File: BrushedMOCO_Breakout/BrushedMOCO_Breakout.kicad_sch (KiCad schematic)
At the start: 24 parts, among them Q1 Si4156DY, Q2 Si4156DY, Q3 Si4156DY, Q4 Si4156DY, U1 74LVC2G04, U2 IRS2308, U5 IRS2308

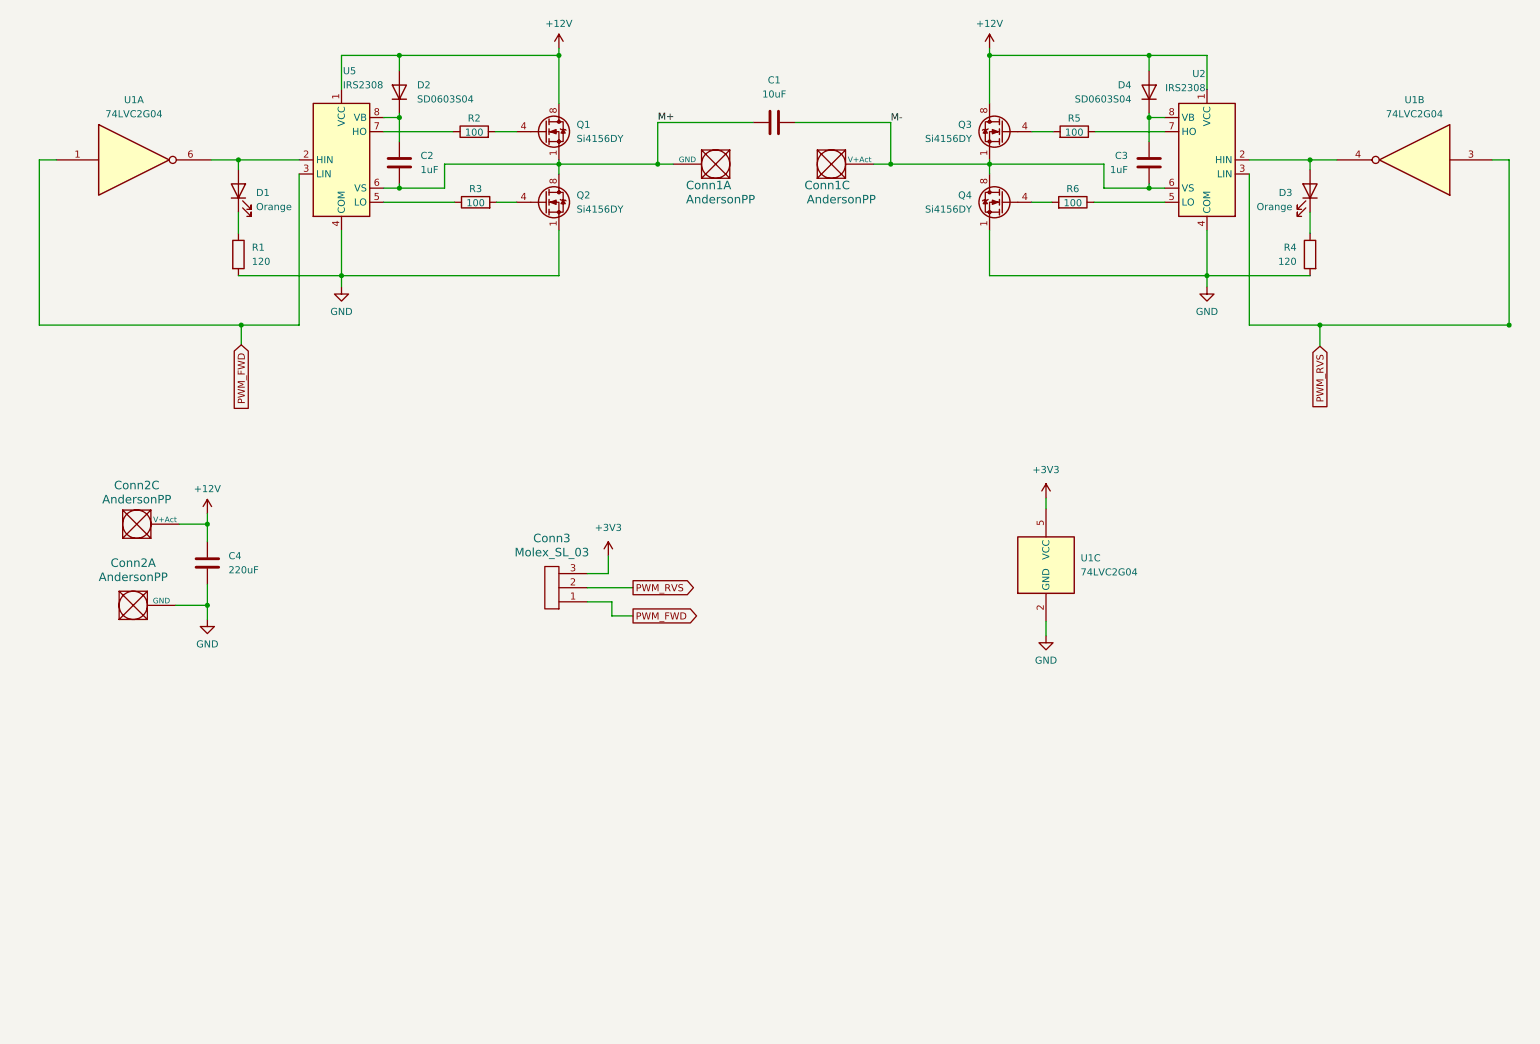
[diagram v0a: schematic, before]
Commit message: Most of Schematic Review Adjustments
This should be all of the schematic review adjustments except for the footprints for the IRS2308. I wasn't sure whether to use
Package_DFN_QFN:Infineon_MLPQ-48-1EP_7x7mm_P0.5mm_EP5.55x5.55mm
or
Package_DFN_QFN:Infineon_MLPQ-48-1EP_7x7mm_P0.5mm_EP5.15x5.15mm
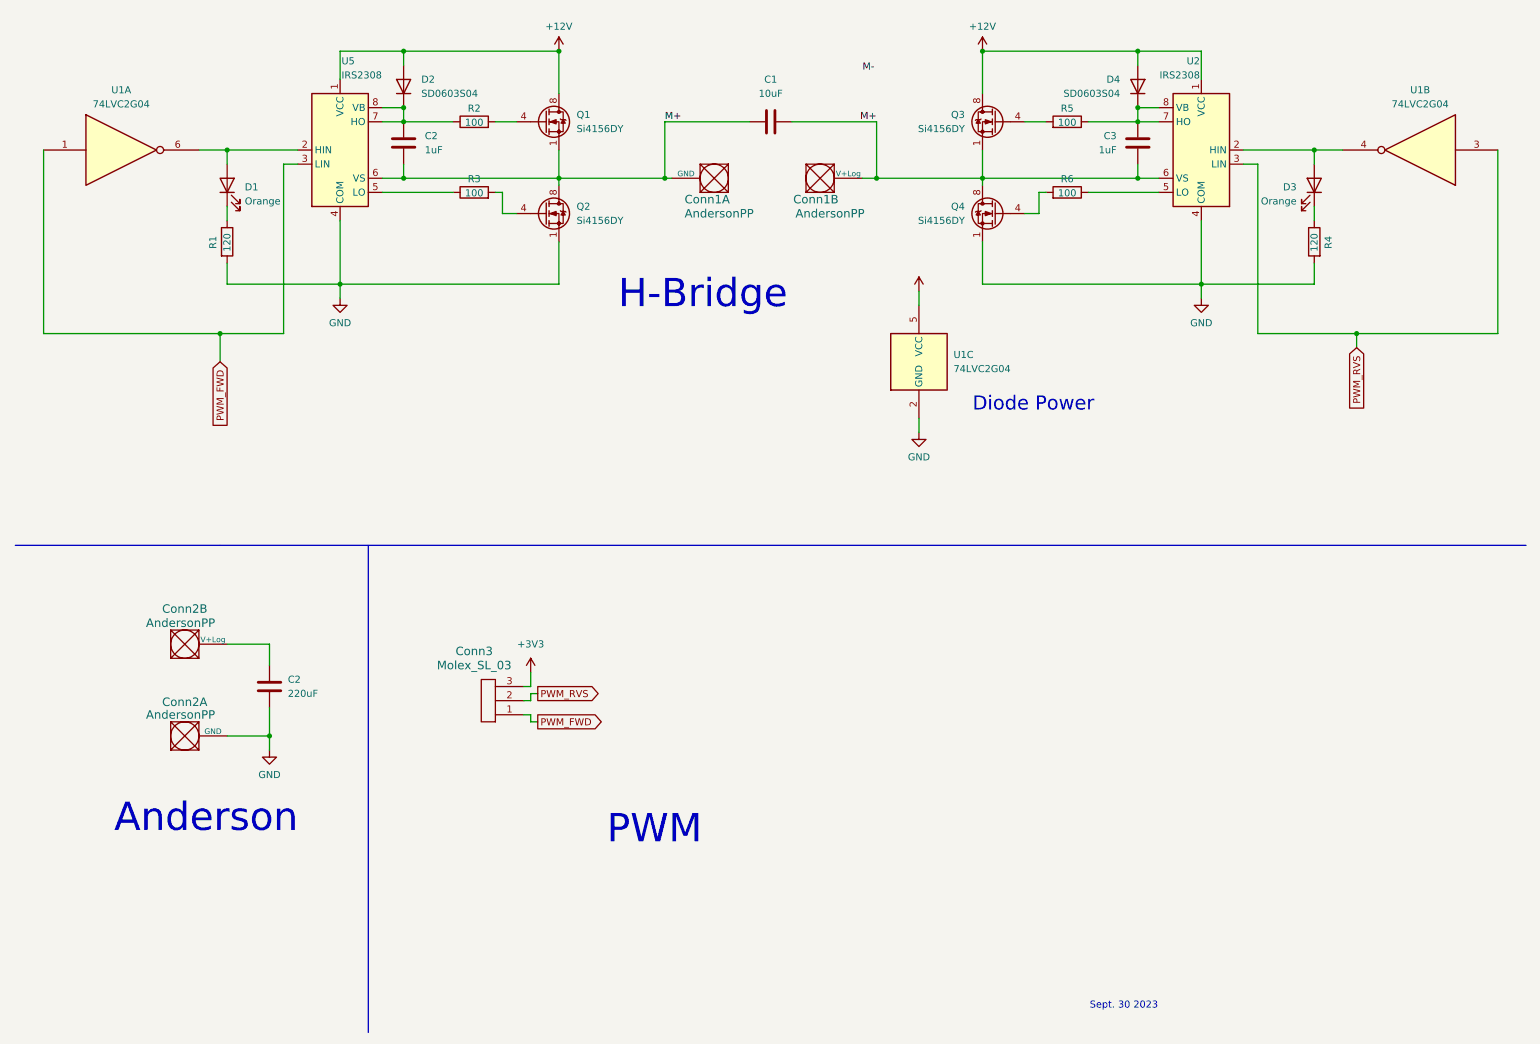
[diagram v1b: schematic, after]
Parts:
- removed unit 3 of Conn2
- added unit 2 of Conn2
- Conn1, Conn2: footprint (none) -> MRDT_Connectors:Square_Anderson_2_H_Side_By_Side_PV
- renumbered C4 to C2
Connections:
- net +12V: no longer C2.2
- net M+: now also C1.2, C3.2, Conn1.2 (V+Log), Q3.1 (S), Q3.2 (S), Q3.3 (S), Q4.5 (D), Q4.6 (D), Q4.7 (D), Q4.8 (D), U2.6 (VS)
- net M-: no longer C1.2, C3.2, Conn1.3 (V+Act), Q3.1 (S), Q3.2 (S), Q3.3 (S), Q4.5 (D), Q4.6 (D), Q4.7 (D), Q4.8 (D), U2.6 (VS)
- net at C2.1, D2.1 (K), U5.8 (VB): now also R2.1, U5.7 (HO)
- net at C3.1, D4.1 (K), U2.8 (VB): now also R5.1, U2.7 (HO)
- new net: C2.2, Conn2.2 (V+Log)
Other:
- note added: "Anderson"
- note added: "Diode Power"
- note added: "H-Bridge"
- note added: "PWM"
- note added: "Sept. 30 2023"
- moved on the sheet: C1, C2, Conn1A, Conn1B, Conn2A, Conn3, D1, D2, Q1, Q2, R1, R2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

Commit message: Finished Footprints
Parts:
- U2: renamed from U5; footprint (none) -> Package_SO:SOIC-8-1EP_3.9x4.9mm_P1.27mm_EP2.29x3mm
- U3: renamed from U2; footprint (none) -> Package_SO:SOIC-8-1EP_3.9x4.9mm_P1.27mm_EP2.29x3mm
- renumbered C2 to C1, C1 to C3, C3 to C4, Conn2 to Conn1, Conn3 to Conn2, Conn1 to Conn3, D4 to D3, D3 to D4, R5 to R4, R6 to R5, R4 to R6
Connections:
- net M+: no longer C3.2, C4.2, Conn3.2 (V+Log), Q3.1 (S), Q3.2 (S), Q3.3 (S), Q4.5 (D), Q4.6 (D), Q4.7 (D), Q4.8 (D), U3.6 (VS)
- net M-: now also C3.2, C4.2, Conn3.2 (V+Log), Q3.1 (S), Q3.2 (S), Q3.3 (S), Q4.5 (D), Q4.6 (D), Q4.7 (D), Q4.8 (D), U3.6 (VS)

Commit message: cleaned up lines
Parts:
- renumbered Conn3 to Conn2
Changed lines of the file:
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@@
     (stroke (width 0) (type default))
   )
-  (polyline (pts (xy 49.53 110.49) (xy 284.48 110.49))
+  (polyline (pts (xy 11.938 109.982) (xy 284.988 109.982))
     (stroke (width 0) (type default))
   )
@@
     (stroke (width 0) (type default))
   )
-  (polyline (pts (xy 12.7 110.49) (xy 49.53 110.49))
-    (stroke (width 0) (type default))
-  )
   (wire (pts (xy 58.42 144.78) (xy 58.42 139.7))
     (stroke (width 0) (type default))
@@
     (stroke (width 0) (type default))
   )
+  (polyline (pts (xy 76.2 197.612) (xy 76.2 197.866))
+    (stroke (width 0) (type default))
+  )
   (wire (pts (xy 218.44 34.29) (xy 214.63 34.29))
     (stroke (width 0) (type default))
@@
     (stroke (width 0) (type default))
   )
-  (polyline (pts (xy 76.2 110.49) (xy 76.2 198.12))
+  (polyline (pts (xy 76.2 109.982) (xy 76.2 197.866))
     (stroke (width 0) (type default))
   )
@@
   )
   (wire (pts (xy 233.68 41.91) (xy 236.22 41.91))
+    (stroke (width 0) (type default))
+  )
+  (polyline (pts (xy 283.972 109.982) (xy 284.988 109.982))
     (stroke (width 0) (type default))
   )
@@
   (symbol (lib_id "MRDT_Connectors:AndersonPP") (at 140.97 41.91 180) (unit 1)
     (in_bom yes) (on_board yes) (dnp no)
-    (property "Reference" "Conn3" (at 133.096 48.26 0)
+    (property "Reference" "Conn2" (at 133.096 48.26 0)
       (effects (font (size 1.524 1.524)) (justify right))
     )
@@
       (project "BrushedMOCO_Breakout"
         (path "/09f10023-b6cf-44c5-8847-9c4a76610e70"
-          (reference "Conn3") (unit 1)
+          (reference "Conn2") (unit 1)
         )
       )
@@
   (symbol (lib_id "MRDT_Connectors:AndersonPP") (at 154.94 46.99 0) (unit 2)
     (in_bom yes) (on_board yes) (dnp no)
-    (property "Reference" "Conn3" (at 156.718 48.26 0)
+    (property "Reference" "Conn2" (at 156.718 48.26 0)
       (effects (font (size 1.524 1.524)))
     )
@@
       (project "BrushedMOCO_Breakout"
         (path "/09f10023-b6cf-44c5-8847-9c4a76610e70"
-          (reference "Conn3") (unit 2)
-        )
-      )
+          (reference "Conn2") (unit 2)
+        )
+      )

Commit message: Saving PCB Progress
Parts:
- renumbered Conn2 to Conn3
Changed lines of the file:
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@@
-    )
-  )
-  (symbol (lib_id "MRDT_Connectors:AndersonPP") (at 140.97 41.91 180) (unit 1)
-    (in_bom yes) (on_board yes) (dnp no)
-    (property "Reference" "Conn2" (at 133.096 48.26 0)
-      (effects (font (size 1.524 1.524)) (justify right))
-    )
-    (property "Value" "AndersonPP" (at 133.096 50.8 0)
-      (effects (font (size 1.524 1.524)) (justify right))
-    )
-    (property "Footprint" "MRDT_Connectors:Square_Anderson_2_H_Side_By_Side_PV" (at 144.78 27.94 0)
-      (effects (font (size 1.524 1.524)) hide)
-    )
-    (property "Datasheet" "" (at 144.78 27.94 0)
-      (effects (font (size 1.524 1.524)) hide)
-    )
-    (pin "1")
-    (pin "2")
-    (pin "3")
-    (pin "4")
-    (pin "1")
-    (instances
-      (project "BrushedMOCO_Breakout"
-        (path "/09f10023-b6cf-44c5-8847-9c4a76610e70"
-          (reference "Conn2") (unit 1)
-        )
-      )
     )
   )
@@
     )
   )
-  (symbol (lib_id "power:+3V3") (at 175.26 64.77 0) (mirror y) (unit 1)
-    (in_bom yes) (on_board yes) (dnp no) (fields_autoplaced)
-    (property "Reference" "#PWR05" (at 175.26 68.58 0)
+  (symbol (lib_id "Device:R") (at 95.25 34.29 90) (unit 1)
+    (in_bom yes) (on_board yes) (dnp no)
+    (property "Reference" "R2" (at 95.25 31.877 90)
+      (effects (font (size 1.27 1.27)))
+    )
+    (property "Value" "100" (at 95.25 34.417 90)
+      (effects (font (size 1.27 1.27)))
+    )
+    (property "Footprint" "Resistor_SMD:R_0603_1608Metric_Pad0.98x0.95mm_HandSolder" (at 95.25 36.068 90)
+      (effects (font (size 1.27 1.27)) hide)
+    )
+    (property "Datasheet" "~" (at 95.25 34.29 0)
+      (effects (font (size 1.27 1.27)) hide)
+    )
+    (pin "1")
+    (pin "2")
+    (instances
+      (project "BrushedMOCO_Breakout"
+        (path "/09f10023-b6cf-44c5-8847-9c4a76610e70"
+          (reference "R2") (unit 1)
+        )
+      )
+    )
+  )
+  (symbol (lib_id "power:GND") (at 175.26 90.17 0) (unit 1)
+    (in_bom yes) (on_board yes) (dnp no) (fields_autoplaced)
+    (property "Reference" "#PWR06" (at 175.26 96.52 0)
+      (effects (font (size 1.27 1.27)) hide)
+    )
+    (property "Value" "GND" (at 175.26 94.615 0)
+      (effects (font (size 1.27 1.27)))
+    )
+    (property "Footprint" "" (at 175.26 90.17 0)
+      (effects (font (size 1.27 1.27)) hide)
+    )
+    (property "Datasheet" "" (at 175.26 90.17 0)
+      (effects (font (size 1.27 1.27)) hide)
+    )
+    (pin "1")
+    (instances
+      (project "BrushedMOCO_Breakout"
+        (path "/09f10023-b6cf-44c5-8847-9c4a76610e70"
+          (reference "#PWR06") (unit 1)
+        )
+      )
+    )
+  )
+  (symbol (lib_id "74xGxx:74LVC2G04") (at 175.26 77.47 0) (unit 3)
+    (in_bom yes) (on_board yes) (dnp no) (fields_autoplaced)
+    (property "Reference" "U1" (at 181.483 76.2 0)
+      (effects (font (size 1.27 1.27)) (justify left))
+    )
+    (property "Value" "74LVC2G04" (at 181.483 78.74 0)
+      (effects (font (size 1.27 1.27)) (justify left))
+    )
+    (property "Footprint" "Package_TO_SOT_SMD:SOT-23-6_Handsoldering" (at 175.26 77.47 0)
+      (effects (font (size 1.27 1.27)) hide)
+    )
+    (property "Datasheet" "http://www.ti.com/lit/sg/scyt129e/scyt129e.pdf" (at 175.26 77.47 0)
+      (effects (font (size 1.27 1.27)) hide)
+    )
+    (pin "1")
+    (pin "6")
+    (pin "3")
+    (pin "4")
+    (pin "2")
+    (pin "5")
+    (instances
+      (project "BrushedMOCO_Breakout"
+        (path "/09f10023-b6cf-44c5-8847-9c4a76610e70"
+          (reference "U1") (unit 3)
+        )
+      )
+    )
+  )
+  (symbol (lib_id "power:+3V3") (at 175.26 64.77 0) (unit 1)
+    (in_bom yes) (on_board yes) (dnp no) (fields_autoplaced)
+    (property "Reference" "#PWR09" (at 175.26 68.58 0)
       (effects (font (size 1.27 1.27)) hide)
     )
     (property "Value" "+3V3" (at 175.26 59.69 0)
-      (effects (font (size 1.27 1.27)) hide)
+      (effects (font (size 1.27 1.27)))
     )
     (property "Footprint" "" (at 175.26 64.77 0)
@@
       (project "BrushedMOCO_Breakout"
         (path "/09f10023-b6cf-44c5-8847-9c4a76610e70"
-          (reference "#PWR05") (unit 1)
-        )
-      )
-    )
-  )
-  (symbol (lib_id "Device:R") (at 95.25 34.29 90) (unit 1)
-    (in_bom yes) (on_board yes) (dnp no)
-    (property "Reference" "R2" (at 95.25 31.877 90)
-      (effects (font (size 1.27 1.27)))
-    )
-    (property "Value" "100" (at 95.25 34.417 90)
-      (effects (font (size 1.27 1.27)))
-    )
-    (property "Footprint" "Resistor_SMD:R_0603_1608Metric_Pad0.98x0.95mm_HandSolder" (at 95.25 36.068 90)
-      (effects (font (size 1.27 1.27)) hide)
-    )
-    (property "Datasheet" "~" (at 95.25 34.29 0)
-      (effects (font (size 1.27 1.27)) hide)
-    )
-    (pin "1")
-    (pin "2")
-    (instances
-      (project "BrushedMOCO_Breakout"
-        (path "/09f10023-b6cf-44c5-8847-9c4a76610e70"
-          (reference "R2") (unit 1)
-        )
-      )
-    )
-  )
-  (symbol (lib_id "power:GND") (at 175.26 90.17 0) (unit 1)
-    (in_bom yes) (on_board yes) (dnp no) (fields_autoplaced)
-    (property "Reference" "#PWR06" (at 175.26 96.52 0)
-      (effects (font (size 1.27 1.27)) hide)
-    )
-    (property "Value" "GND" (at 175.26 94.615 0)
-      (effects (font (size 1.27 1.27)))
-    )
-    (property "Footprint" "" (at 175.26 90.17 0)
-      (effects (font (size 1.27 1.27)) hide)
-    )
-    (property "Datasheet" "" (at 175.26 90.17 0)
-      (effects (font (size 1.27 1.27)) hide)
-    )
-    (pin "1")
-    (instances
-      (project "BrushedMOCO_Breakout"
-        (path "/09f10023-b6cf-44c5-8847-9c4a76610e70"
-          (reference "#PWR06") (unit 1)
-        )
-      )
-    )
-  )
-  (symbol (lib_id "74xGxx:74LVC2G04") (at 175.26 77.47 0) (unit 3)
-    (in_bom yes) (on_board yes) (dnp no) (fields_autoplaced)
-    (property "Reference" "U1" (at 181.483 76.2 0)
-      (effects (font (size 1.27 1.27)) (justify left))
-    )
-    (property "Value" "74LVC2G04" (at 181.483 78.74 0)
-      (effects (font (size 1.27 1.27)) (justify left))
-    )
-    (property "Footprint" "Package_TO_SOT_SMD:SOT-23-6_Handsoldering" (at 175.26 77.47 0)
-      (effects (font (size 1.27 1.27)) hide)
-    )
-    (property "Datasheet" "http://www.ti.com/lit/sg/scyt129e/scyt129e.pdf" (at 175.26 77.47 0)
-      (effects (font (size 1.27 1.27)) hide)
-    )
-    (pin "1")
-    (pin "6")
-    (pin "3")
-    (pin "4")
-    (pin "2")
-    (pin "5")
-    (instances
-      (project "BrushedMOCO_Breakout"
-        (path "/09f10023-b6cf-44c5-8847-9c4a76610e70"
-          (reference "U1") (unit 3)
+          (reference "#PWR09") (unit 1)
         )
       )
@@
     )
   )
+  (symbol (lib_id "MRDT_Connectors:AndersonPP") (at 140.97 41.91 180) (unit 1)
+    (in_bom yes) (on_board yes) (dnp no)
+    (property "Reference" "Conn2" (at 133.858 48.26 0)
+      (effects (font (size 1.524 1.524)) (justify right))
+    )
+    (property "Value" "AndersonPP" (at 133.858 50.8 0)
+      (effects (font (size 1.524 1.524)) (justify right))
+    )
+    (property "Footprint" "MRDT_Connectors:Square_Anderson_2_H_Side_By_Side_PV" (at 144.78 27.94 0)
+      (effects (font (size 1.524 1.524)) hide)
+    )
+    (property "Datasheet" "" (at 144.78 27.94 0)
+      (effects (font (size 1.524 1.524)) hide)
+    )
+    (pin "1")
+    (pin "2")
+    (pin "3")
+    (pin "4")
+    (pin "1")
+    (instances
+      (project "BrushedMOCO_Breakout"
+        (path "/09f10023-b6cf-44c5-8847-9c4a76610e70"
+          (reference "Conn2") (unit 1)
+        )
+      )
+    )
+  )
   (symbol (lib_id "Driver_FET:IRS2308") (at 226.06 39.37 0) (mirror y) (unit 1)
     (in_bom yes) (on_board yes) (dnp no)
@@
     )
   )
+  (symbol (lib_id "MRDT_Connectors:AndersonPP") (at 154.94 46.99 0) (unit 2)
+    (in_bom yes) (on_board yes) (dnp no)
+    (property "Reference" "Conn2" (at 157.734 48.26 0)
+      (effects (font (size 1.524 1.524)))
+    )
+    (property "Value" "AndersonPP" (at 157.734 50.8 0)
+      (effects (font (size 1.524 1.524)))
+    )
+    (property "Footprint" "MRDT_Connectors:Square_Anderson_2_H_Side_By_Side_PV" (at 151.13 60.96 0)
+      (effects (font (size 1.524 1.524)) hide)
+    )
+    (property "Datasheet" "" (at 151.13 60.96 0)
+      (effects (font (size 1.524 1.524)) hide)
+    )
+    (pin "1")
+    (pin "2")
+    (pin "3")
+    (pin "4")
+    (pin "1")
+    (instances
+      (project "BrushedMOCO_Breakout"
+        (path "/09f10023-b6cf-44c5-8847-9c4a76610e70"
+          (reference "Conn2") (unit 2)
+        )
+      )
+    )
+  )
   (symbol (lib_id "Driver_FET:IRS2308") (at 71.12 39.37 0) (unit 1)
     (in_bom yes) (on_board yes) (dnp no)
@@
   (symbol (lib_id "MRDT_Connectors:Molex_SL_03") (at 99.06 134.62 180) (unit 1)
     (in_bom yes) (on_board yes) (dnp no)
-    (property "Reference" "Conn2" (at 95.25 129.54 0)
+    (property "Reference" "Conn3" (at 95.25 129.54 0)
       (effects (font (size 1.524 1.524)))
     )
@@
       (project "BrushedMOCO_Breakout"
         (path "/09f10023-b6cf-44c5-8847-9c4a76610e70"
-          (reference "Conn2") (unit 1)
+          (reference "Conn3") (unit 1)
         )
       )
@@
         )
       )
-    )
-  )
-  (symbol (lib_id "MRDT_Connectors:AndersonPP") (at 154.94 46.99 0) (unit 2)
-    (in_bom yes) (on_board yes) (dnp no)
-    (property "Reference" "Conn2" (at 156.718 48.26 0)
-      (effects (font (size 1.524 1.524)))
-    )
-    (property "Value" "AndersonPP" (at 159.258 50.8 0)
-      (effects (font (size 1.524 1.524)))
-    )
-    (property "Footprint" "MRDT_Connectors:Square_Anderson_2_H_Side_By_Side_PV" (at 151.13 60.96 0)
-      (effects (font (size 1.524 1.524)) hide)
-    )
-    (property "Datasheet" "" (at 151.13 60.96 0)
-      (effects (font (size 1.524 1.524)) hide)
-    )
-    (pin "1")
-    (pin "2")
-    (pin "3")
-    (pin "4")
-    (pin "1")
-    (instances
-      (project "BrushedMOCO_Breakout"
-        (path "/09f10023-b6cf-44c5-8847-9c4a76610e70"
-          (reference "Conn2") (unit 2)
-        )
-      )
